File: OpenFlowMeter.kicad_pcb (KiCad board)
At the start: 2 copper layers, 19 parts, among them Q1 BC856, U1 LT1492, U2 STM32F103C8Tx, U3 MCP4725xxx-xCH, U4 ADS1115IDGS

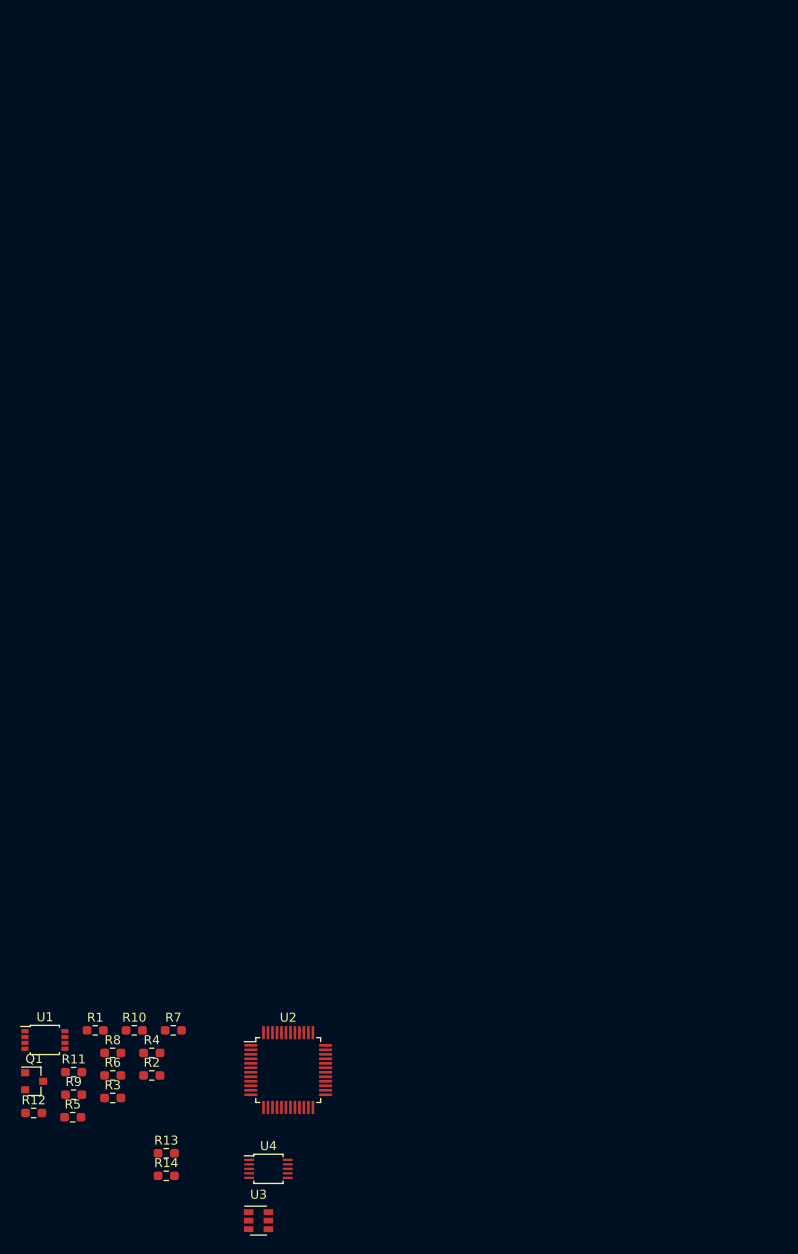
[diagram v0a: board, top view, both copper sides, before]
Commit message: Layout CH2 & 100n deboucing Cs
Copied layout from Channel 1 to Channel 2 and added 100n Cs to +24V rails
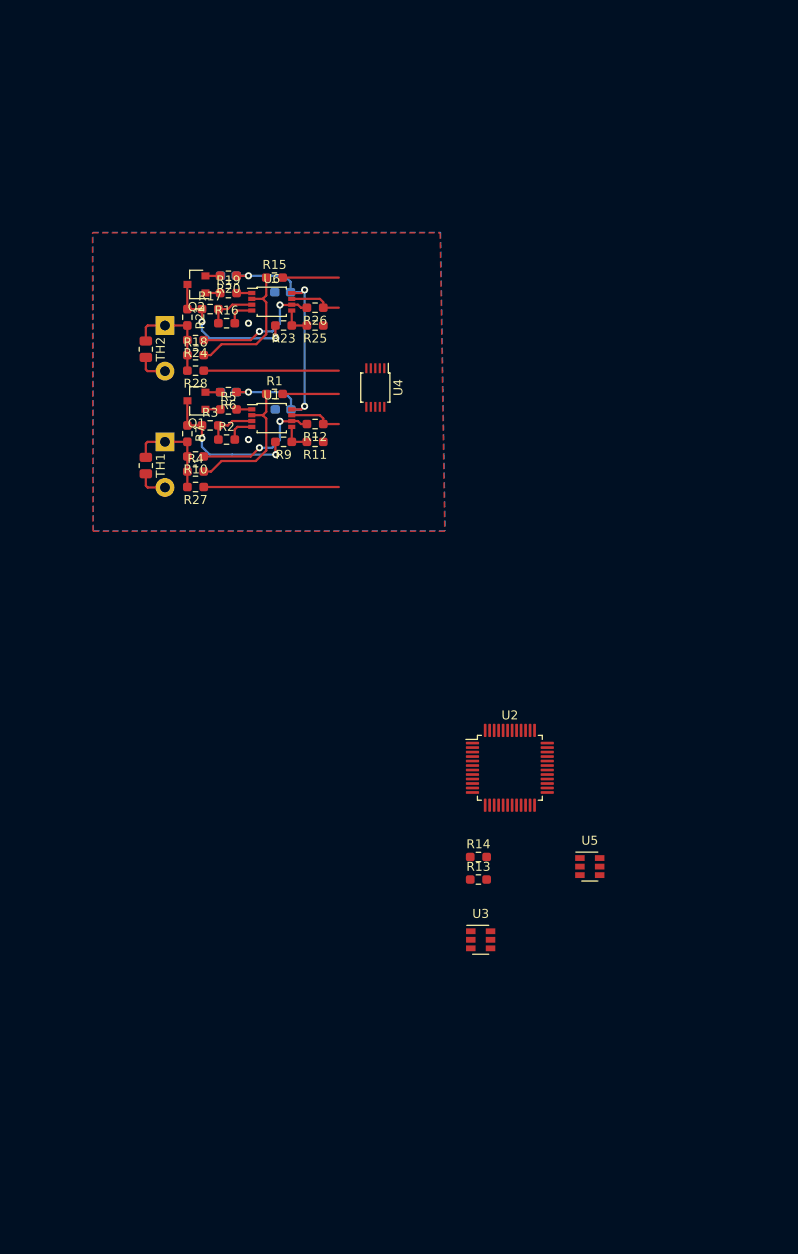
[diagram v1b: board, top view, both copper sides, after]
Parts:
- removed R8: 100, Resistor_SMD:R_0603_1608Metric_Pad0.98x0.95mm_HandSolder
- added C1: C, Capacitor_SMD:C_0603_1608Metric_Pad1.05x0.95mm_HandSolder, B.Cu at (114.7, -10.9)
- added C2: C, Capacitor_SMD:C_0603_1608Metric_Pad1.05x0.95mm_HandSolder, B.Cu at (120.8, -8.99)
- added C3: C, Capacitor_SMD:C_0603_1608Metric_Pad1.05x0.95mm_HandSolder, B.Cu at (114.7, -23.9)
- added C4: C, Capacitor_SMD:C_0603_1608Metric_Pad1.05x0.95mm_HandSolder, B.Cu at (120.7, -22.0)
- added J1: Screw_Terminal_01x02, TerminalBlock_RND:TerminalBlock_RND_205-00232_1x02_P5.08mm_Horizontal, B.Cu at (107.6, -5.38)
- added J2: Screw_Terminal_01x02, TerminalBlock_RND:TerminalBlock_RND_205-00232_1x02_P5.08mm_Horizontal, B.Cu at (107.6, -18.3)
- added Q2: BC856, Package_TO_SOT_SMD:SOT-23, F.Cu at (111.1, -22.9)
- added R15: 1k, Resistor_SMD:R_0603_1608Metric_Pad0.98x0.95mm_HandSolder, F.Cu at (119.8, -23.7)
- added R16: 47k, Resistor_SMD:R_0603_1608Metric_Pad0.98x0.95mm_HandSolder, F.Cu at (114.5, -18.6)
- added R17: 47k, Resistor_SMD:R_0603_1608Metric_Pad0.98x0.95mm_HandSolder, F.Cu at (112.6, -20.2)
- added R18: 47k, Resistor_SMD:R_0603_1608Metric_Pad0.98x0.95mm_HandSolder, F.Cu at (111.0, -15.0)
- added R19: 100, Resistor_SMD:R_0603_1608Metric_Pad0.98x0.95mm_HandSolder, F.Cu at (114.7, -21.9)
- added R20: 47, Resistor_SMD:R_0603_1608Metric_Pad0.98x0.95mm_HandSolder, F.Cu at (114.7, -23.9)
- added R21: 220, Resistor_SMD:R_0603_1608Metric_Pad0.98x0.95mm_HandSolder, F.Cu at (110.1, -19.3)
- added R23: 22k, Resistor_SMD:R_0603_1608Metric_Pad0.98x0.95mm_HandSolder, F.Cu at (120.8, -18.3)
- added R24: 22k, Resistor_SMD:R_0603_1608Metric_Pad0.98x0.95mm_HandSolder, F.Cu at (111.0, -16.7)
- added R25: 10k, Resistor_SMD:R_0603_1608Metric_Pad0.98x0.95mm_HandSolder, F.Cu at (124.3, -18.3)
- added R26: 10k, Resistor_SMD:R_0603_1608Metric_Pad0.98x0.95mm_HandSolder, F.Cu at (124.3, -20.3)
- added R27: 1k, Resistor_SMD:R_0603_1608Metric_Pad0.98x0.95mm_HandSolder, F.Cu at (111.0, -0.36)
- added R28: 1k, Resistor_SMD:R_0603_1608Metric_Pad0.98x0.95mm_HandSolder, F.Cu at (111.0, -13.3)
- added TH1: PT100, Resistor_SMD:R_0805_2012Metric, F.Cu at (105.5, -2.74)
- added TH2: PT100, Resistor_SMD:R_0805_2012Metric, F.Cu at (105.5, -15.7)
- added U5: MCP4725xxx-xCH, Package_TO_SOT_SMD:SOT-23-6, F.Cu at (154.9, 41.9)
- added U6: LT1492, Package_SO:OnSemi_Micro8, F.Cu at (119.5, -21.0)
- moved U4 87.8 mm to (131.0, -11.4), turned to 270 degrees
- moved R12 82.9 mm to (124.3, -7.37), turned to 180 degrees
- moved R5 80.7 mm to (114.7, -8.99)
- moved Q1 77.9 mm to (111.1, -9.96), turned to 180 degrees
- moved R6 77.2 mm to (114.7, -10.9), turned to 180 degrees
- moved R9 76.4 mm to (120.8, -5.38), turned to 180 degrees
- moved R3 75.7 mm to (112.6, -7.21)
- moved R11 75.1 mm to (124.3, -5.38), turned to 180 degrees
- moved U1 73.7 mm to (119.5, -8.03)
- moved R1 73.6 mm to (119.8, -10.7)
- moved R2 71.3 mm to (114.5, -5.64)
- moved R7 66.5 mm to (110.1, -6.30), turned to 270 degrees
- moved R4 64.9 mm to (111.0, -2.08)
- moved R10 64.3 mm to (111.0, -3.76), turned to 180 degrees
- moved R14 49.7 mm to (142.5, 40.8)
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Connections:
- net /CurrentSource/IMEAS renamed /CurrentSource 1/IMEAS
- net /CurrentSource/ISET renamed /CurrentSource 1/ISET
- net 0 renamed GND
- R10 pad 2: /ADC/IN1 -> /CurrentSource 1/Iout
- R4 pad 1: /ADC/IN1 -> /CurrentSource 1/Iout
- R7 pad 2: /ADC/IN1 -> /CurrentSource 1/Iout
- U4 pad 6: /ADC/IN2 -> /Current Source 2/IMEAS
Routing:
- net +24V: track 0.00 -> 37.1 mm, vias 0 -> 4
- net Net-(Q1-Pad3): track 0.00 -> 16.8 mm, vias 0 -> 2
- net Net-(Q2-Pad3): track 0.00 -> 16.8 mm, vias 0 -> 2
- net Net-(R15-Pad1): track 0.00 -> 15.8 mm
- net Net-(R1-Pad1): track 0.00 -> 15.8 mm
- net /ADC/IN3: track 0.00 -> 15.0 mm
- net /ADC/IN1: track 0.00 -> 15.0 mm
- net Net-(R24-Pad1): track 0.00 -> 14.5 mm, vias 0 -> 2
- net Net-(R10-Pad1): track 0.00 -> 14.5 mm, vias 0 -> 2
- net GND: track 0.00 -> 13.6 mm, vias 0 -> 2
- net /CurrentSource 1/Iout: track 0.00 -> 11.2 mm
- net /Current Source 2/Iout: track 0.00 -> 11.2 mm
- net /CurrentSource 1/ISET: track 0.00 -> 6.25 mm
- net /Current Source 2/ISET: track 0.00 -> 6.25 mm
- net /CurrentSource 1/IMEAS: track 0.00 -> 6.01 mm
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- added copper zone on B.Cu, net GND
- added copper zone on F.Cu, net GND

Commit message: Added passive filtering
passive filtering to smoothen the analog voltage instead of real DAC.
Using PWM and the ADC inside the microcontroller reduces the number of components.
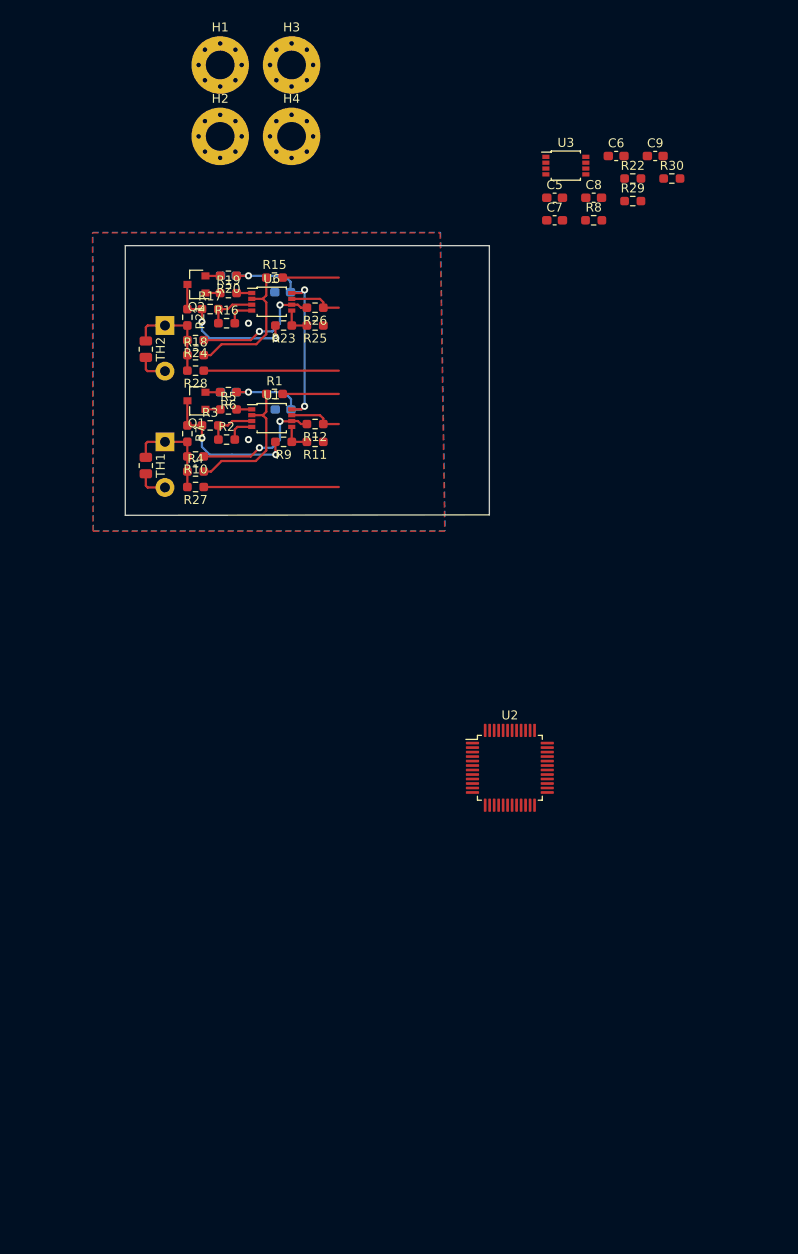
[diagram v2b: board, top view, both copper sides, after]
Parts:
- removed R13, R14: 10k, Resistor_SMD:R_0603_1608Metric_Pad0.98x0.95mm_HandSolder
- removed U4: ADS1115IDGS, Package_SO:TSSOP-10_3x3mm_P0.5mm
- removed U5: MCP4725xxx-xCH, Package_TO_SOT_SMD:SOT-23-6
- added C5: C, Capacitor_SMD:C_0603_1608Metric_Pad1.05x0.95mm_HandSolder, F.Cu at (151.0, -32.6)
- added C6: C, Capacitor_SMD:C_0603_1608Metric_Pad1.05x0.95mm_HandSolder, F.Cu at (157.8, -37.2)
- added C7: C, Capacitor_SMD:C_0603_1608Metric_Pad1.05x0.95mm_HandSolder, F.Cu at (151.0, -30.1)
- added C8: C, Capacitor_SMD:C_0603_1608Metric_Pad1.05x0.95mm_HandSolder, F.Cu at (155.3, -32.6)
- added C9: C, Capacitor_SMD:C_0603_1608Metric_Pad1.05x0.95mm_HandSolder, F.Cu at (162.2, -37.2)
- added H1: MountingHole_Pad, MountingHole:MountingHole_3.2mm_M3_Pad_Via, F.Cu at (113.7, -47.3)
- added H2: MountingHole_Pad, MountingHole:MountingHole_3.2mm_M3_Pad_Via, F.Cu at (113.7, -39.4)
- added H3: MountingHole_Pad, MountingHole:MountingHole_3.2mm_M3_Pad_Via, F.Cu at (121.7, -47.3)
- added H4: MountingHole_Pad, MountingHole:MountingHole_3.2mm_M3_Pad_Via, F.Cu at (121.7, -39.4)
- added R22: 1k, Resistor_SMD:R_0603_1608Metric_Pad0.98x0.95mm_HandSolder, F.Cu at (159.7, -34.7)
- added R29: 1k, Resistor_SMD:R_0603_1608Metric_Pad0.98x0.95mm_HandSolder, F.Cu at (159.7, -32.2)
- added R30: 1k, Resistor_SMD:R_0603_1608Metric_Pad0.98x0.95mm_HandSolder, F.Cu at (164.0, -34.7)
- added R8: 1k, Resistor_SMD:R_0603_1608Metric_Pad0.98x0.95mm_HandSolder, F.Cu at (155.3, -30.1)
- U3: value MCP4725xxx-xCH -> LT1492; footprint Package_TO_SOT_SMD:SOT-23-6 -> Package_SO:OnSemi_Micro8
- moved U3 86.7 mm to (152.2, -36.1)
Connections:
- R27 pad 1: /ADC/IN1 -> /CurrentSource 1/UMEAS
- R28 pad 1: /ADC/IN3 -> /Current Source 2/UMEAS
- U3 pad 2: Net-(U3-Pad2) -> /CurrentSource 1/ISET
- U3 pad 4: /SDA -> GND
- U3 pad 5: /SCL -> Net-(C8-Pad1)
- U3 pad 6: Net-(U3-Pad6) -> /Current Source 2/ISET
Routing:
- net /CurrentSource 1/UMEAS: track 0.00 -> 15.0 mm
- net /Current Source 2/UMEAS: track 0.00 -> 15.0 mm
- net /ADC/IN3: track 15.0 -> 0.00 mm
- net /ADC/IN1: track 15.0 -> 0.00 mm
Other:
- board outline added: 40.5 x 30 mm
- board text added: "Ch. 1"
- board text added: "Ch. 2"

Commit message: Changed to KiCAD v6
opened and converted project to KiCAD version 6
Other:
- net class Default removed

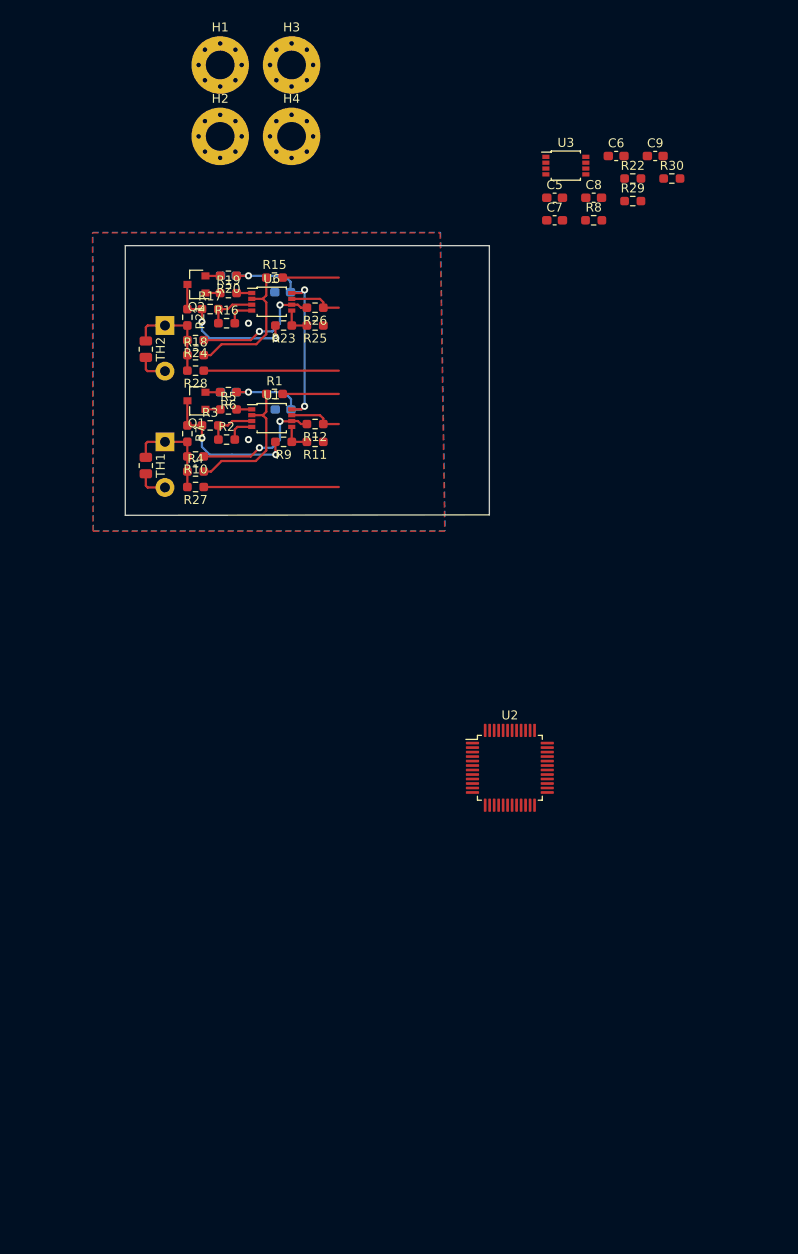
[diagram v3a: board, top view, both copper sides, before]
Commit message: intermediate commit
updated schematics and started with controller section

layout proceeded with PWM filter
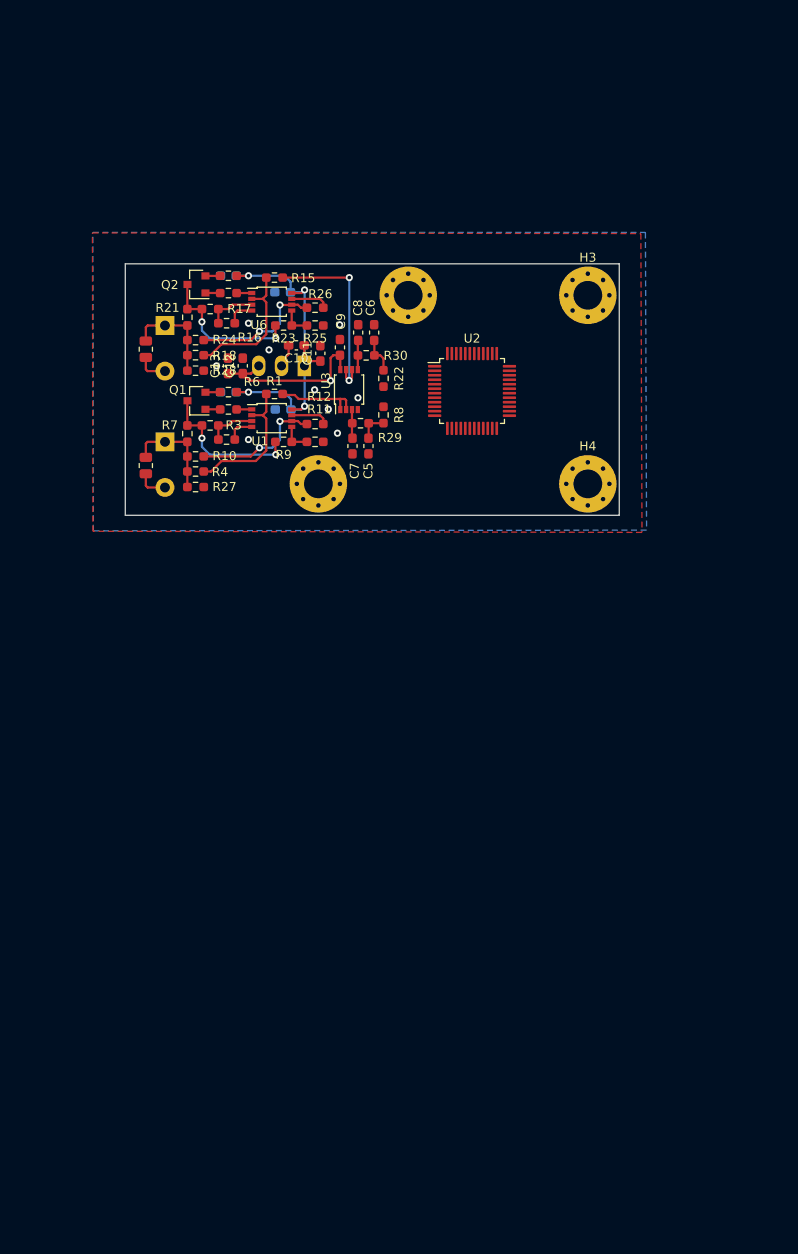
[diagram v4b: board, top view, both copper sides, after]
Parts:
- added C10: C, Capacitor_SMD:C_0603_1608Metric_Pad1.08x0.95mm_HandSolder, F.Cu at (122.2, -16.1)
- added C11: C, Capacitor_SMD:C_0603_1608Metric_Pad1.08x0.95mm_HandSolder, F.Cu at (124.9, -15.2)
- added C12: C, Capacitor_SMD:C_0603_1608Metric_Pad1.08x0.95mm_HandSolder, F.Cu at (116.3, -13.8)
- added C13: C, Capacitor_SMD:C_0603_1608Metric_Pad1.08x0.95mm_HandSolder, F.Cu at (114.6, -13.8)
- added U4: R-78C3.3-1.0, Converter_DCDC:Converter_DCDC_RECOM_R-78E-0.5_THT, B.Cu at (123.1, -13.8)
- moved H4 50.8 mm to (154.7, -0.71)
- moved H1 47.9 mm to (124.7, -0.71)
- moved U2 42.2 mm to (141.8, -11.0)
- moved H3 41.8 mm to (154.7, -21.7)
- moved C9 41.1 mm to (127.1, -15.9), turned to 90 degrees
- moved R30 39.3 mm to (130.0, -15.0)
- moved R29 39.1 mm to (129.4, -7.46)
- moved R22 35.6 mm to (131.9, -12.4), turned to -90 degrees
- moved U3 34.7 mm to (128.1, -11.2), turned to 90 degrees
- moved C5 34.6 mm to (130.2, -4.92), turned to -90 degrees
- moved C7 33.7 mm to (128.5, -4.92), turned to -90 degrees
- moved C6 33.4 mm to (130.9, -17.6), turned to 90 degrees
- moved R8 31.9 mm to (131.9, -8.38), turned to 90 degrees
- moved C8 30.2 mm to (129.1, -17.6), turned to 90 degrees
- moved H2 27.4 mm to (134.7, -21.7)
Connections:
- net /CurrentSource 1/IMEAS renamed /Current Source 1/IMEAS
- net /CurrentSource 1/ISET renamed /Current Source 1/ISET
- net /CurrentSource 1/Iout renamed /Current Source 1/Iout
- net /CurrentSource 1/UMEAS renamed /Current Source 1/UMEAS
- U2 pad 1: Net-(U2-Pad1) -> +3V3
- U2 pad 10: Net-(U2-Pad10) -> unconnected-(U2-Pad10)
- U2 pad 11: Net-(U2-Pad11) -> unconnected-(U2-Pad11)
- U2 pad 12: Net-(U2-Pad12) -> unconnected-(U2-Pad12)
- U2 pad 13: Net-(U2-Pad13) -> unconnected-(U2-Pad13)
- U2 pad 14: Net-(U2-Pad14) -> unconnected-(U2-Pad14)
- U2 pad 15: Net-(U2-Pad15) -> unconnected-(U2-Pad15)
- U2 pad 16: Net-(U2-Pad16) -> unconnected-(U2-Pad16)
- U2 pad 17: Net-(U2-Pad17) -> unconnected-(U2-Pad17)
- U2 pad 18: Net-(U2-Pad18) -> unconnected-(U2-Pad18)
- U2 pad 19: Net-(U2-Pad19) -> unconnected-(U2-Pad19)
- U2 pad 2: Net-(U2-Pad2) -> unconnected-(U2-Pad2)
- U2 pad 20: Net-(U2-Pad20) -> unconnected-(U2-Pad20)
- U2 pad 21: Net-(U2-Pad21) -> unconnected-(U2-Pad21)
- U2 pad 22: Net-(U2-Pad22) -> unconnected-(U2-Pad22)
- U2 pad 23: Net-(U2-Pad23) -> GND
- U2 pad 24: Net-(U2-Pad24) -> +3V3
- U2 pad 25: Net-(U2-Pad25) -> unconnected-(U2-Pad25)
- U2 pad 26: Net-(U2-Pad26) -> unconnected-(U2-Pad26)
- U2 pad 27: Net-(U2-Pad27) -> unconnected-(U2-Pad27)
- U2 pad 28: Net-(U2-Pad28) -> unconnected-(U2-Pad28)
- U2 pad 29: Net-(U2-Pad29) -> unconnected-(U2-Pad29)
- U2 pad 3: Net-(U2-Pad3) -> unconnected-(U2-Pad3)
- U2 pad 30: Net-(U2-Pad30) -> unconnected-(U2-Pad30)
- U2 pad 31: Net-(U2-Pad31) -> unconnected-(U2-Pad31)
- U2 pad 32: Net-(U2-Pad32) -> unconnected-(U2-Pad32)
- U2 pad 33: Net-(U2-Pad33) -> unconnected-(U2-Pad33)
- U2 pad 34: Net-(U2-Pad34) -> unconnected-(U2-Pad34)
- U2 pad 35: Net-(U2-Pad35) -> GND
- U2 pad 36: Net-(U2-Pad36) -> +3V3
- U2 pad 37: Net-(U2-Pad37) -> unconnected-(U2-Pad37)
- U2 pad 38: Net-(U2-Pad38) -> unconnected-(U2-Pad38)
- U2 pad 39: Net-(U2-Pad39) -> unconnected-(U2-Pad39)
- U2 pad 4: Net-(U2-Pad4) -> unconnected-(U2-Pad4)
- U2 pad 40: Net-(U2-Pad40) -> unconnected-(U2-Pad40)
- U2 pad 41: Net-(U2-Pad41) -> unconnected-(U2-Pad41)
- U2 pad 42: Net-(U2-Pad42) -> unconnected-(U2-Pad42)
- U2 pad 43: Net-(U2-Pad43) -> unconnected-(U2-Pad43)
- U2 pad 44: Net-(U2-Pad44) -> unconnected-(U2-Pad44)
- U2 pad 45: Net-(U2-Pad45) -> unconnected-(U2-Pad45)
- U2 pad 46: Net-(U2-Pad46) -> unconnected-(U2-Pad46)
- U2 pad 47: Net-(U2-Pad47) -> GND
- U2 pad 48: Net-(U2-Pad48) -> +3V3
- U2 pad 5: Net-(U2-Pad5) -> unconnected-(U2-Pad5)
- U2 pad 6: Net-(U2-Pad6) -> unconnected-(U2-Pad6)
- U2 pad 7: Net-(U2-Pad7) -> unconnected-(U2-Pad7)
- U2 pad 8: Net-(U2-Pad8) -> GND
- U2 pad 9: Net-(U2-Pad9) -> +3V3
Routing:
- net +3V3: track 0.00 -> 19.5 mm, vias 0 -> 1
- net /Current Source 2/ISET: track 6.25 -> 21.5 mm, vias 0 -> 2
- net /Current Source 2/UMEAS: track 15.0 -> 0.00 mm
- net /Current Source 1/UMEAS: track 15.0 -> 0.00 mm
- net +24V: track 37.1 -> 41.4 mm
- net Net-(C6-Pad1): track 0.00 -> 4.14 mm
- net Net-(C7-Pad1): track 0.00 -> 3.40 mm
- net Net-(C8-Pad1): track 0.00 -> 3.39 mm
- net /Current Source 1/ISET: track 6.25 -> 9.63 mm
- net Net-(C5-Pad1): track 0.00 -> 3.28 mm
- net GND: track 13.6 -> 16.3 mm, vias 2 -> 9
- net /Current Source 2/IMEAS: track 6.01 -> 4.28 mm
- net /Current Source 1/IMEAS: track 6.01 -> 4.28 mm
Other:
- board size 40.5 x 30 mm -> 55 x 28 mm
